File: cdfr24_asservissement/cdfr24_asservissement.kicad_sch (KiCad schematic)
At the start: 64 parts, among them J1 Connecteur batterie, J10 Free Connecteur, J11 Conn_01x02, J12 Conn_01x02, J13 Connecteur Odométrie, J14 Conn_ST_STDC14, J2 Conn_01x03, J3 Conn_01x05, J4 Connecteur Programmation, J5 Conn_01x03, J6 Connecteur Odométrie, J7 Conn_01x03, Q13 Q_NMOS_GDS, U1 LM317_SOT-223, U3 STM32F401RCTx, U4 LMR16020PDDA, U4 LSM6DSL, Y1 Crystal_GND24

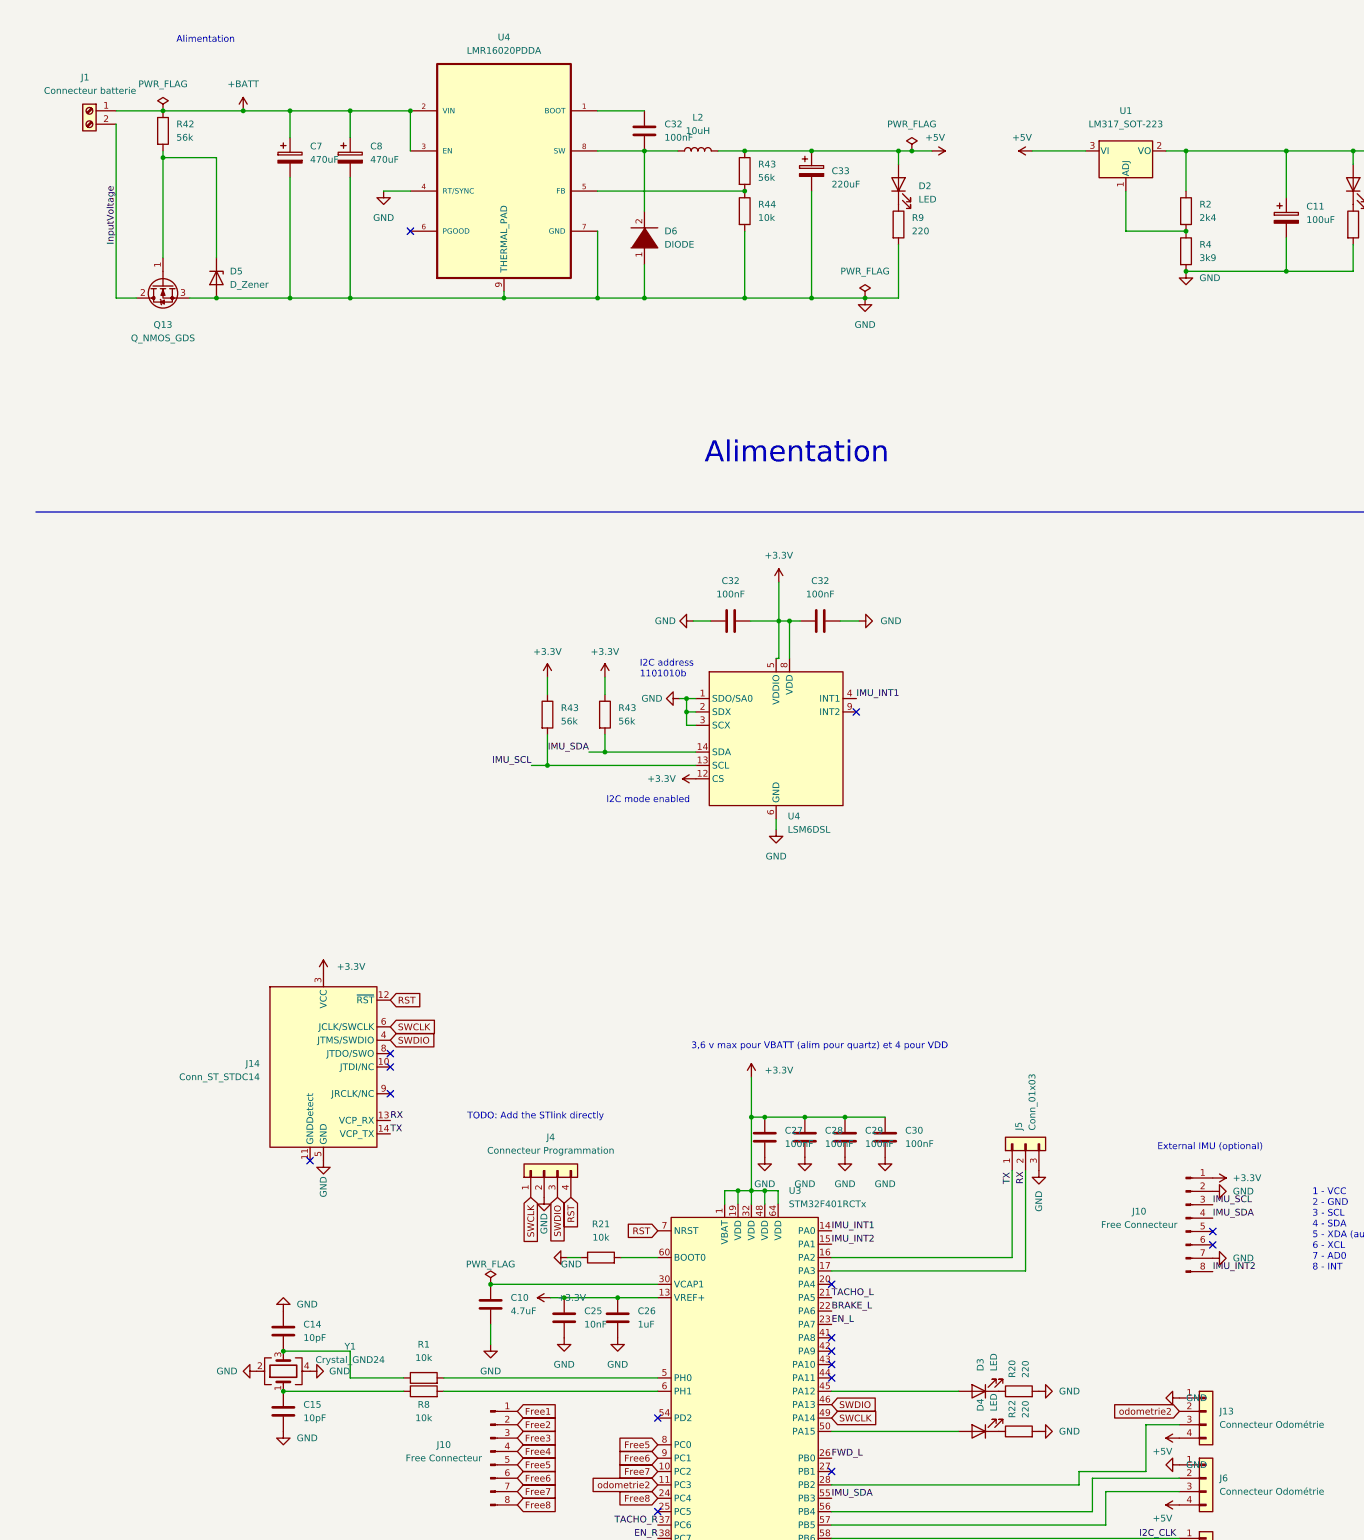
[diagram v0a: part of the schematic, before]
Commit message: Add new components
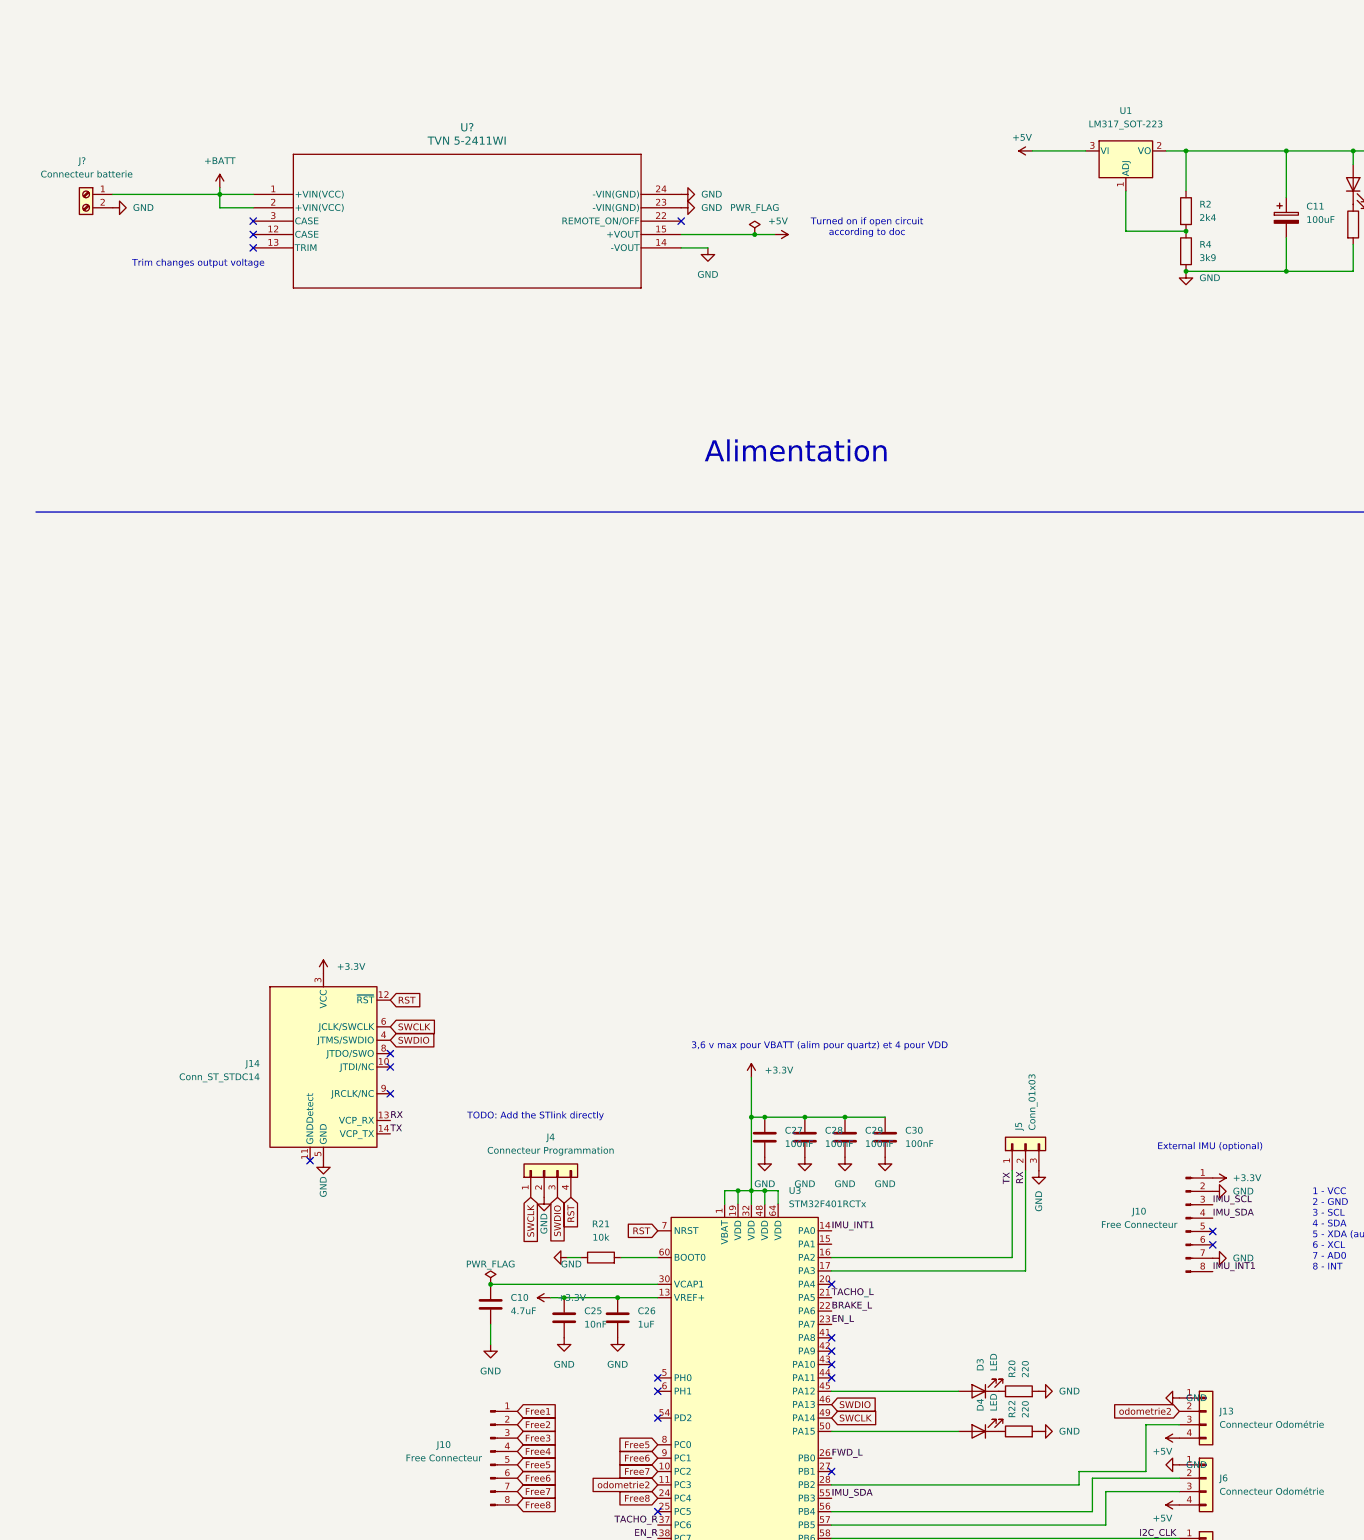
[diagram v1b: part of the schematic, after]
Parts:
- removed C14, C15: 10pF, Capacitor_SMD:C_0805_2012Metric_Pad1.18x1.45mm_HandSolder, symbol Device:C
- removed C32 (x3): 100nF, Capacitor_SMD:C_0805_2012Metric_Pad1.18x1.45mm_HandSolder, symbol Device:C
- removed C33: 220uF, Capacitor_SMD:CP_Elec_10x10.5, symbol Device:C_Polarized
- removed C7, C8: 470uF, Capacitor_SMD:CP_Elec_10x10.5, symbol Device:C_Polarized
- removed D2: LED, LED_SMD:LED_0805_2012Metric_Pad1.15x1.40mm_HandSolder, symbol Device:LED
- removed D5: D_Zener, Diode_SMD:D_SOD-123, symbol Device:D_Zener
- removed D6: DIODE, B170B:DIOM505270X240, symbol pspice:DIODE
- removed J1: Connecteur batterie, TerminalBlockBend:CUI_TBP01R1-508-02BE, symbol Connector:Screw_Terminal_01x02
- removed L2: 10uH, IHLP2525CZER100M01:IND_IHLP_2525_CZ-M, symbol Device:L
- removed Q13: Q_NMOS_GDS, Package_TO_SOT_SMD:TO-252-2, symbol Device:Q_NMOS_GDS
- removed R1, R44, R8: 10k, Resistor_SMD:R_0805_2012Metric_Pad1.20x1.40mm_HandSolder, symbol Device:R
- removed R42, R43 (x3): 56k, Resistor_SMD:R_0805_2012Metric_Pad1.20x1.40mm_HandSolder, symbol Device:R
- removed R9: 220, Resistor_SMD:R_0805_2012Metric_Pad1.20x1.40mm_HandSolder, symbol Device:R
- removed U4: LSM6DSL, Package_LGA:LGA-14_3x2.5mm_P0.5mm_LayoutBorder3x4y, symbol Sensor_Motion:LSM6DSL
- removed U4: LMR16020PDDA, Package_SO:SOIC-8-1EP_3.9x4.9mm_P1.27mm_EP2.41x3.3mm, symbol LMR16020PDDA:LMR16020PDDA
- removed Y1: Crystal_GND24, Crystal:Crystal_SMD_2520-4Pin_2.5x2.0mm, symbol Device:Crystal_GND24
- added J?: Connecteur batterie, TerminalBlockBend:CUI_TBP01R1-508-02BE, symbol Connector:Screw_Terminal_01x02
- added U?: TVN 5-2411WI, TVN_5WI_SINGLE_TRP:TVN_5WI_SINGLE_TRP, symbol TVN-5-2411WI:TVN_5-2411WI
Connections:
- net +5V: now also U?.15 (+VOUT)
- net +BATT: now also J?.1 (Pin_1), U?.1 (+VIN(VCC)), U?.2 (+VIN(VCC))
- net GND: now also J?.2 (Pin_2), U?.14 (-VOUT), U?.23 (-VIN(GND)), U?.24 (-VIN(GND))
- net IMU_INT1: now also J10.8 (Pin_8)
- net IMU_INT2: no longer names the net of U3.15 (PA1)
- net IMU_INT2: no longer J10.8 (Pin_8)
- no-connect marks 22 -> 26
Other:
- note added: "Trim changes output voltage"
- note added: "Turned on if open circuit according to doc"
- note removed: "I2C address 1101010b"
- note removed: "I2C mode enabled"

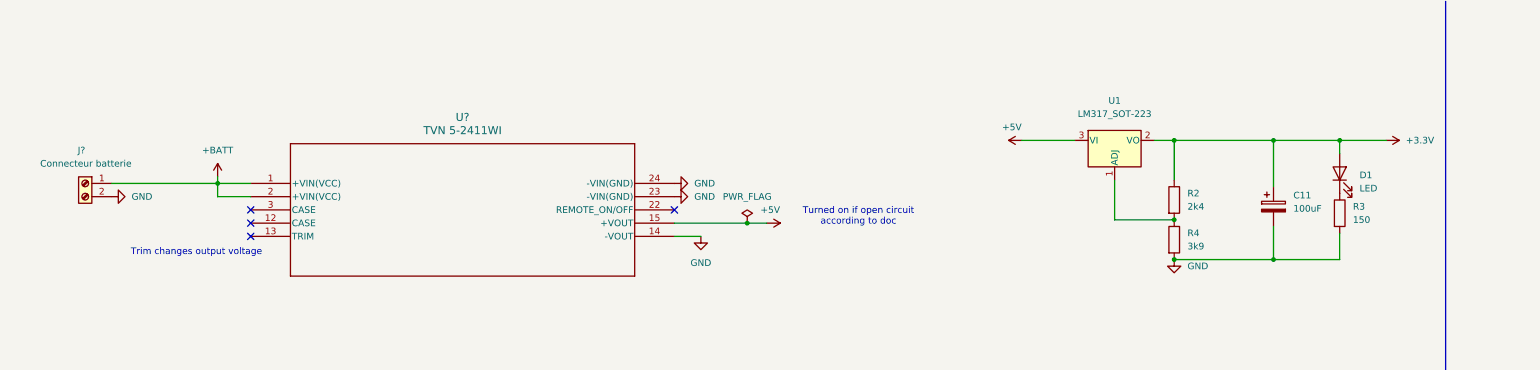
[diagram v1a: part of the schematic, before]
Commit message: Change 5v to 3.3v regulator to ST product
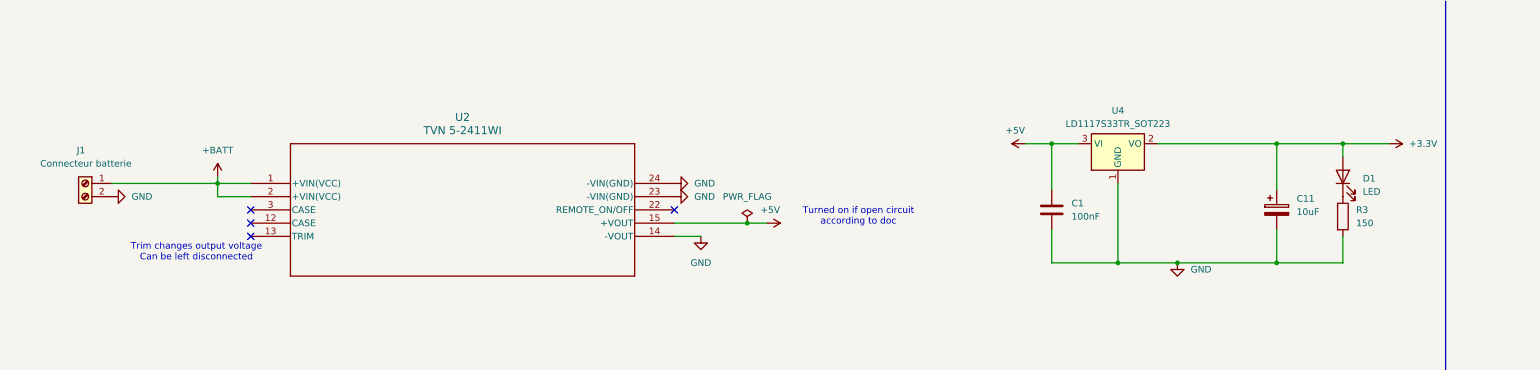
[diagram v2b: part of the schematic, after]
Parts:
- removed R2: 2k4, Resistor_SMD:R_0805_2012Metric_Pad1.20x1.40mm_HandSolder, symbol Device:R
- removed R4: 3k9, Resistor_SMD:R_0805_2012Metric_Pad1.20x1.40mm_HandSolder, symbol Device:R
- removed U1: LM317_SOT-223, Package_TO_SOT_SMD:SOT-223-3_TabPin2, symbol Regulator_Linear:LM317_SOT-223
- added C1: 100nF, symbol Device:C
- added U4: LD1117S33TR_SOT223, Package_TO_SOT_SMD:SOT-223-3_TabPin2, symbol Regulator_Linear:LD1117S33TR_SOT223
- C11: value 100uF -> 10uF
- gave numbers to parts that had none: 2
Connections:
- net +3.3V: now also U4.2 (VO)
- net +5V: now also C1.1, U4.3 (VI)
- net GND: now also C1.2, U4.1 (GND)
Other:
- note added: "Trim changes output voltage Can be left disconnected"
- note removed: "Trim changes output voltage"
- moved on the sheet: C11, D1, R3

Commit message: Realign elements to grid
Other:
- note added: "External IMU"
- note added: "STLINK"
- note removed: "External IMU (optional)"
- moved on the sheet: C10, C25, C26, C27, C28, C29, C30, D3, D4, J10, J11, J12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

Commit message: Combine charge pump
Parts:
- added C13: 10n, Capacitor_SMD:C_0805_2012Metric_Pad1.18x1.45mm_HandSolder, symbol Device:C
- added C14, C3, C4: 100n, Capacitor_SMD:C_0805_2012Metric_Pad1.18x1.45mm_HandSolder, symbol Device:C
- added C2: 100u, Capacitor_SMD:CP_Elec_10x10.5, symbol Device:C
- added D1, D4: DIODE, B170B:DIOM505270X240, symbol pspice:DIODE
- added D3: D_Zener, Diode_SMD:D_SOD-123, symbol Device:D_Zener
- added F1: 01550900M, LittleFuse:FUSE_01550900M_LTF, symbol LittleFuse:01550900M
- added NT1: NetTie_2, NetTie:NetTie-2_SMD_Pad2.0mm, symbol Device:NetTie_2
- added Q1: Q_NMOS_GDS, Package_TO_SOT_SMD:TO-252-2, symbol Device:Q_NMOS_GDS
- added R1: 56k, Resistor_SMD:R_0805_2012Metric_Pad1.20x1.40mm_HandSolder, symbol Device:R
- added R2: 100, Resistor_SMD:R_0805_2012Metric_Pad1.20x1.40mm_HandSolder, symbol Device:R
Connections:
- net +BATT: now also F1.1, R1.1
- net GND: now also NT1.2; no longer J1.2 (Pin_2), U2.23 (-VIN(GND)), U2.24 (-VIN(GND))
- net Vref_DAC: now reaches U3.41 (PA8)
- new net: D3.1 (K), Q1.1 (G), R1.2
- new net: C13.1, R2.2
- new net: D1.2 (A), D4.1 (K), R2.1
- new net: J1.2 (Pin_2), Q1.2 (D)
- new net GNDPWR: C2.2, C3.2, D3.2 (A), NT1.1, Q1.3 (S), U2.23 (-VIN(GND)), U2.24 (-VIN(GND))
- new net Vboot: C14.2, C4.2, D4.2 (A)
- new net Vcp_L: C13.2
- new net Vsab: C14.1, C2.1, C3.1, C4.1, D1.1 (K), F1.2
- no-connect marks 26 -> 27
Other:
- sheet left_driver ports: added Vboot, Vcp, Vref_analog, Vsab; removed none
- sheet right_driver ports: added Vboot, Vcp, Vref_analog, Vsab; removed none
- note added: "Each 100n capacitor should be connected between Vsab and Vboot as close as possible"
- note added: "IMPORTANT: STM32 pins are 5V tolerant however, GPIO needs to have NO PULL UP AND NO PULL DOWN in the pin configuration"
- note added: "Point that connects Power ground and signal ground protect signal ground from the noise"
- note added: "Power ground and signal ground connect here"
- note added: "Reverse voltage protection"
- note removed: "Speed control pin"
- moved on the sheet: H2, H3, H4, J2, J3, U2

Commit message: Change STM32 pins
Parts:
- removed J4: Connecteur Programmation, Connector_PinHeader_2.54mm:PinHeader_1x04_P2.54mm_Vertical, symbol Connector_Generic:Conn_01x04
- added C15: 100u, Capacitor_SMD:CP_Elec_10x10.5, symbol Device:C_Polarized
- C2: value 100u -> 220u; symbol Device:C -> Device:C_Polarized
- J2: symbol Connector_Generic:Conn_01x03 -> Connector:Screw_Terminal_01x03
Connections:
- net +5V: now also C15.1
- net BRAKE_L: now also U3.36 (PB15); no longer U3.22 (PA6)
- net BRAKE_R: now also U3.28 (PB2); no longer U3.36 (PB15)
- net EN_L: now also U3.35 (PB14); no longer U3.23 (PA7)
- net EN_R: now also U3.27 (PB1); no longer U3.38 (PC7)
- net FWD_L: now also U3.42 (PA9); no longer U3.26 (PB0)
- net FWD_R: now also U3.43 (PA10); no longer U3.34 (PB13)
- net Free1: no longer U3.62 (PB9)
- net Free5: no longer U3.8 (PC0)
- net Free6: no longer U3.9 (PC1)
- net Free7: no longer U3.10 (PC2)
- net Free8: no longer U3.24 (PC4)
- net GND: now also C15.2; no longer J10.7 (Pin_7)
- net I2C_CLK: now also U3.61 (PB8); no longer U3.58 (PB6)
- net I2C_SDA: now also U3.62 (PB9); no longer U3.59 (PB7)
- net IMU_SCL: now also U3.41 (PA8); no longer U3.29 (PB10)
- net IMU_SDA: now also U3.40 (PC9); no longer U3.55 (PB3)
- net TACHO_L: now also U3.37 (PC6); no longer U3.21 (PA5)
- net TACHO_R: now also U3.29 (PB10); no longer U3.37 (PC6)
- net Vref_DAC: now also U3.44 (PA11); no longer U3.41 (PA8)
- net at J13.3 (Pin_3): now also U3.15 (PA1); no longer U3.28 (PB2)
- net at J6.2 (Pin_2): now also U3.58 (PB6); no longer U3.56 (PB4)
- net at J6.3 (Pin_3): now also U3.59 (PB7); no longer U3.57 (PB5)
- net SWO: now reaches J14.8 (JTDO/SWO)
- net SWO: now also U3.55 (PB3)
- net IMU_INT1: no longer names the net of U3.14 (PA0)
- net IMU_INT1: now also J13.2 (Pin_2); no longer J10.8 (Pin_8)
- net odometrie2 renamed INT_IMU
- net INT_IMU: now also J10.8 (Pin_8); no longer J13.2 (Pin_2)
- new net INT_MAG: J10.7 (Pin_7), U3.24 (PC4)
- no-connect marks 27 -> 29
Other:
- note added: "1 - VCC 2 - GND 3 - SCL 4 - SDA 5 - XDA (auxiliary I2C communication) 6 - XCL 7 - INT_MAG / AD0 for MPU 8 - INT_IMU"
- note removed: "1 - VCC 2 - GND 3 - SCL 4 - SDA 5 - XDA (auxiliary I2C communication) 6 - XCL 7 - AD0 8 - INT"
- note removed: "TODO: Add the STlink directly"
- moved on the sheet: C10, C25, C26, C27, C28, C29, C30, D3, D4, J10, J11, J12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

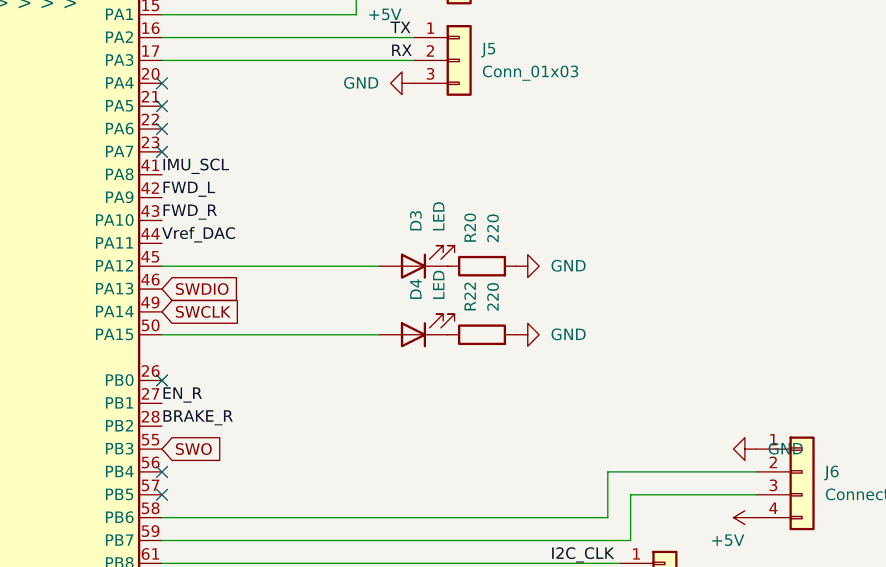
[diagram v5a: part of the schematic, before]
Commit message: Add low pass filter
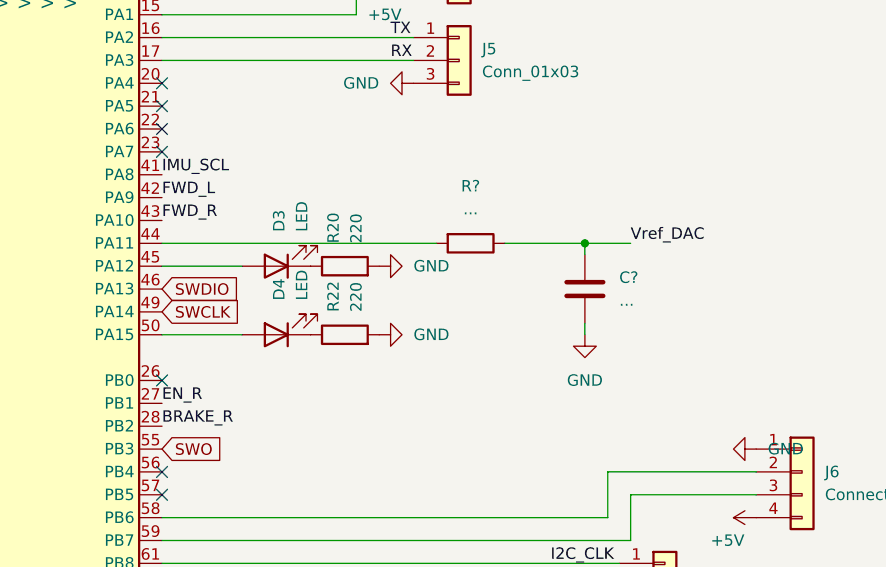
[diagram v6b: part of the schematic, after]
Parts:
- added C?: ..., Capacitor_SMD:C_0805_2012Metric_Pad1.18x1.45mm_HandSolder, symbol Device:C
- added R?: ..., Resistor_SMD:R_0805_2012Metric_Pad1.20x1.40mm_HandSolder, symbol Device:R
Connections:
- net GND: now also C?.2
- net Vref_DAC: now also C?.1, R?.1; no longer U3.44 (PA11)
- new net: R?.2, U3.44 (PA11)
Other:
- moved on the sheet: D3, D4, R20, R22
